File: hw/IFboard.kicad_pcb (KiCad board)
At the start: 2 copper layers, 110 x 65.1 mm, 99 parts, among them J1 USB_C_Receptacle_USB2.0_16P, J10 IcoTec_36650.2, J2 Phoenix_1881561, J3 Conn_ARM_SWD_TagConnect_TC203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, J4 Phoenix_1881561, J5 Phoenix_1881561, J6 Phoenix_1881561, J7 IcoTec_36650.2, J8 IcoTec_36650.2, J9 IcoTec_36650.2, SW3 SW_Push, SW4 SW_Push, SW5 SW_Push, SW6 SW_Push, U2 XC6206P332MR-G, U3 TCAN3413DR, U4 ST4E1240DT, U5 MAX232ESE+T, U6 STM32G0B1CBTx, U7 ER_OLEDM0.91_1x-I2C

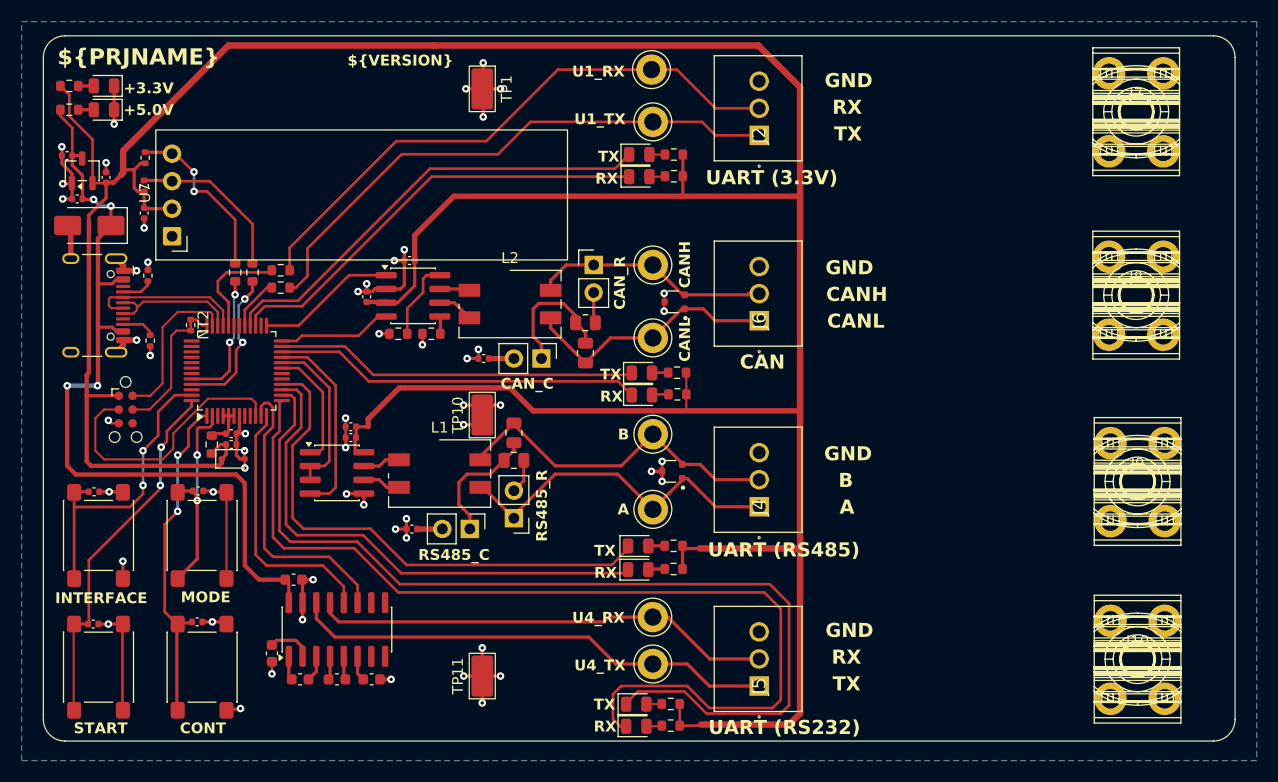
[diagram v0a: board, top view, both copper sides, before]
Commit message: added jumpers to be able to short CMCs
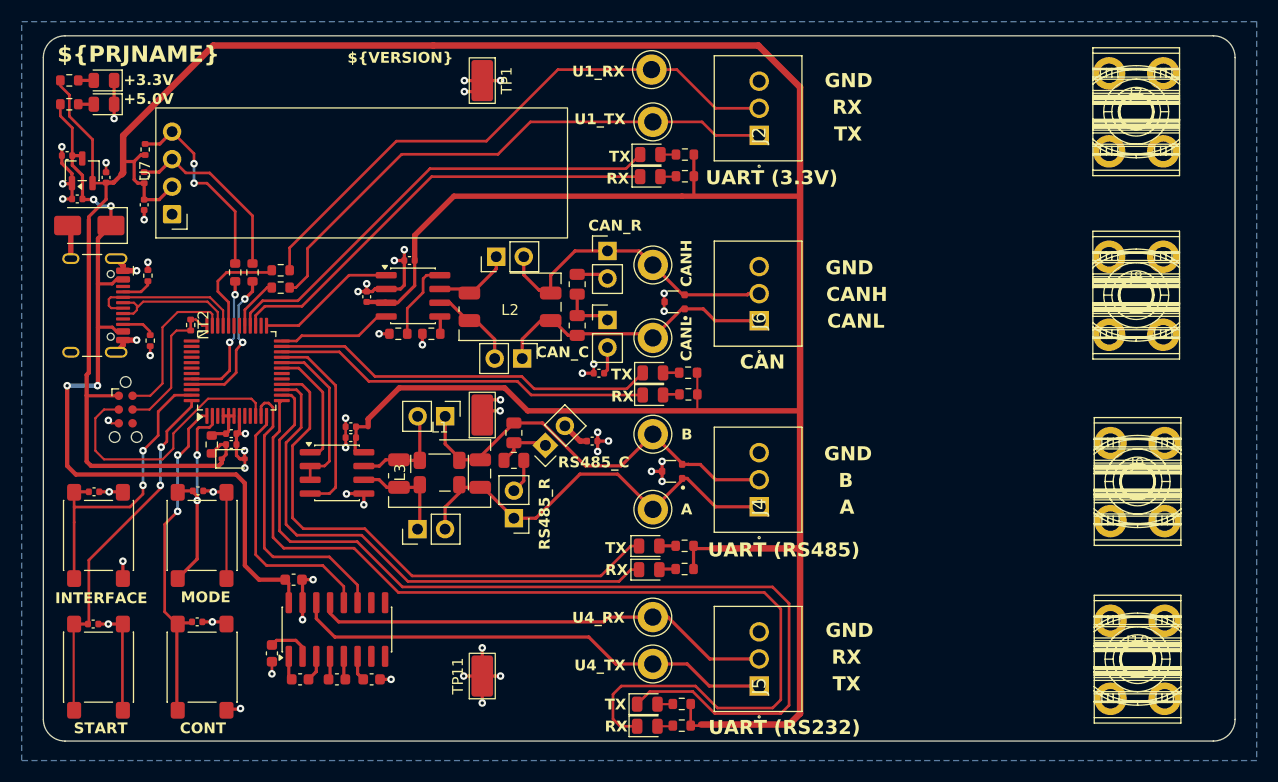
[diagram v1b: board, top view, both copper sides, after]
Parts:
- added JP5: Jumper_2_Open, Connector_PinHeader_2.54mm:PinHeader_1x02_P2.54mm_Vertical, F.Cu at (85.5, 95.9)
- added JP6: Jumper_2_Open, Connector_PinHeader_2.54mm:PinHeader_1x02_P2.54mm_Vertical, F.Cu at (88.0, 85.5)
- added JP7: Jumper_2_Open, Connector_PinHeader_2.54mm:PinHeader_1x02_P2.54mm_Vertical, F.Cu at (92.7, 70.7)
- added JP8: Jumper_2_Open, Connector_PinHeader_2.54mm:PinHeader_1x02_P2.54mm_Vertical, F.Cu at (95.1, 80.1)
- added L3: 100 uH, PZ:L_Wurth_WE-CNSW-1812, F.Cu at (87.5, 90.6)
- moved C24 18.5 mm to (101.6, 87.7), turned to 180 degrees
- moved C20 10.7 mm to (102.2, 81.5)
- moved JP3 10.4 mm to (97.3, 88.1), turned to 135 degrees
- moved JP4 7.06 mm to (103.0, 76.6), turned to 0 degrees
- moved R14 3.64 mm to (100.2, 73.3), turned to -90 degrees
- moved R15 2.65 mm to (100.2, 77.1)
- moved U7 2.03 mm to (62.8, 66.8)
- moved JP2 1.82 mm to (103.0, 70.2)
- moved D10 1.02 mm to (106.8, 99.6)
- moved D6 1.02 mm to (107.2, 81.4)
- moved D8 1.02 mm to (107.2, 83.5)
- moved D9 1.02 mm to (106.8, 97.4)
- moved R10 1.02 mm to (110.1, 61.3)
- moved R11 1.02 mm to (110.1, 63.3)
- moved R13 1.02 mm to (110.5, 83.4)
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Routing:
- net Net-(JP4-A): track 12.4 -> 4.69 mm
- net GND: track 115.2 -> 107.8 mm, vias 55 -> 53
- net Net-(JP3-A): track 11.7 -> 5.01 mm
- net Net-(J4-Pin_2): track 32.1 -> 38.7 mm
- net Net-(J4-Pin_1): track 32.7 -> 39.2 mm
- net Net-(JP5-A): track 3.54 -> 9.75 mm
- net Net-(J6-Pin_2): track 21.9 -> 28.0 mm
- net Net-(JP6-B): track 3.48 -> 9.57 mm
- net Net-(JP8-B): track 3.31 -> 8.24 mm
- net Net-(JP7-A): track 2.78 -> 7.56 mm
- net Net-(J6-Pin_1): track 24.0 -> 26.9 mm
- net /SDA: track 16.0 -> 18.3 mm
- net /CAN_TX_LED: track 33.5 -> 35.5 mm
- net /USART3_TX_LED: track 48.5 -> 50.5 mm
- net /SCL: track 15.2 -> 17.1 mm
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
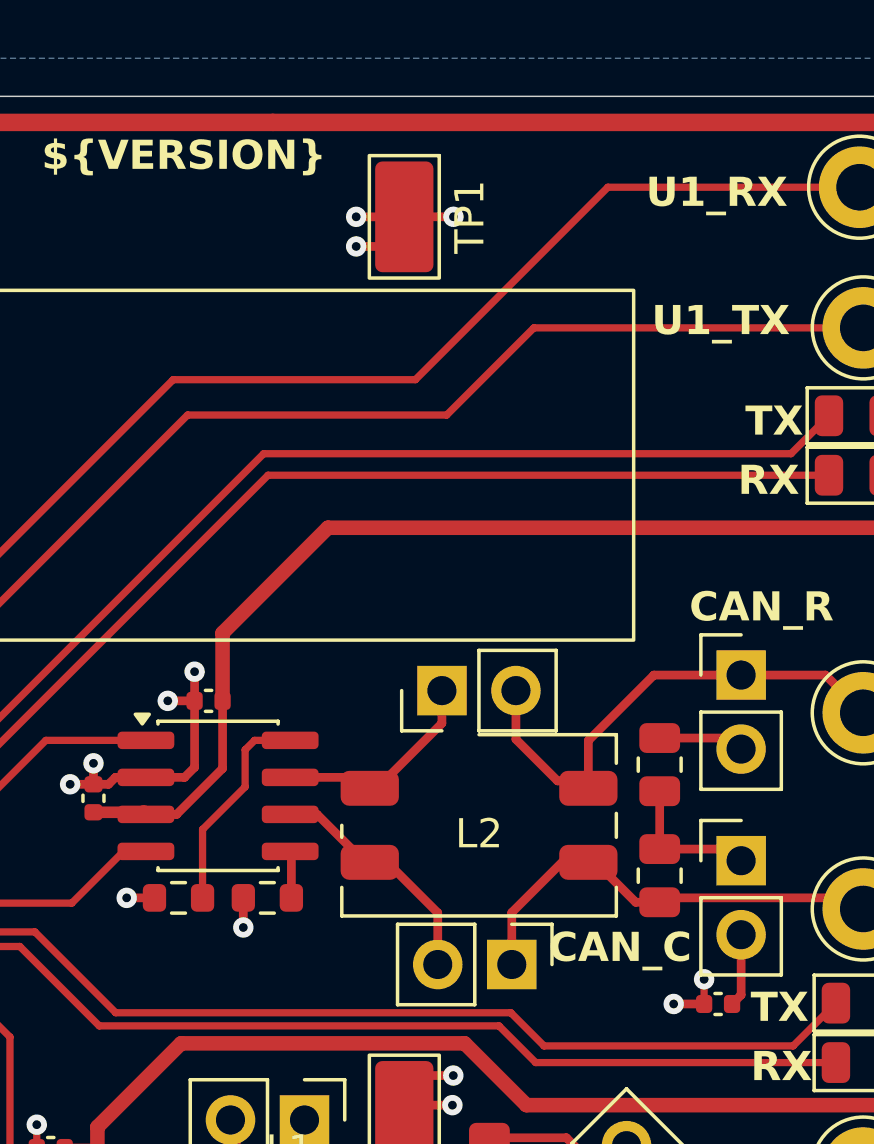
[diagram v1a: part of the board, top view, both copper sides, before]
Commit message: corrected rotation offsets for JLC
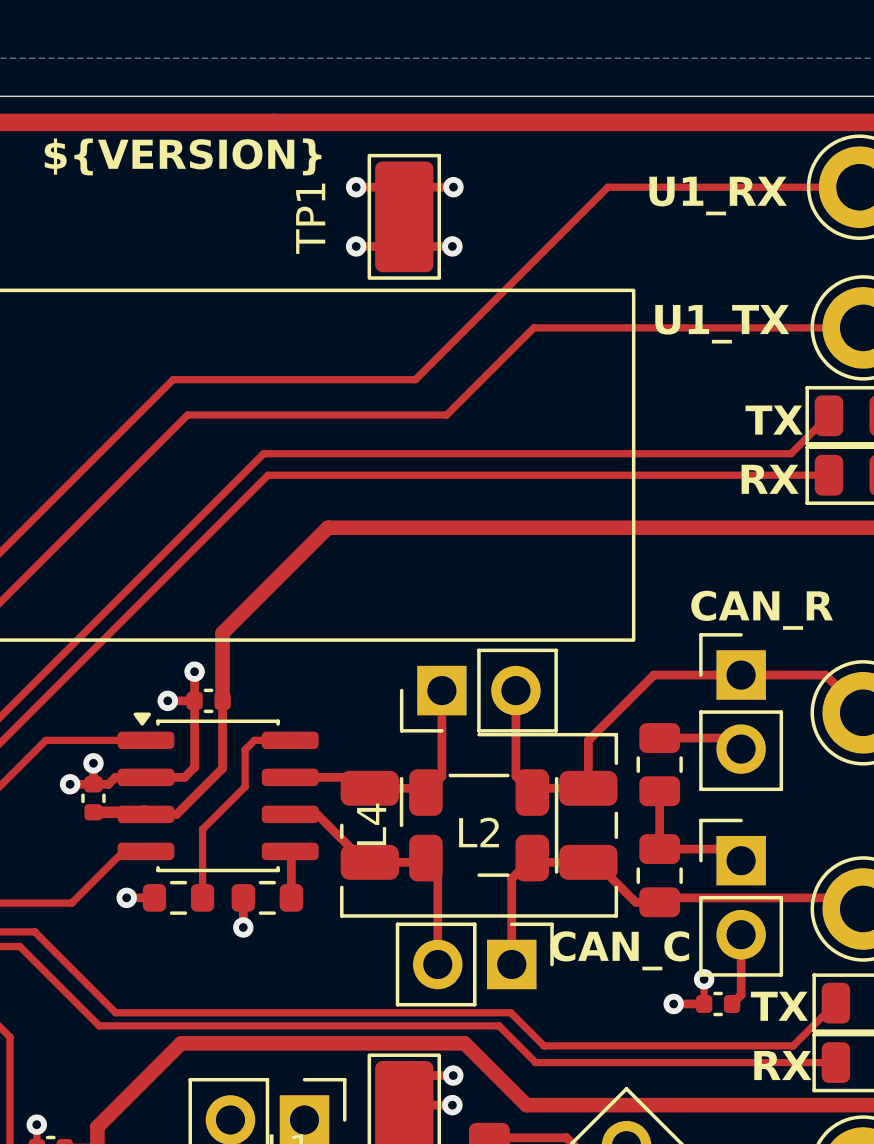
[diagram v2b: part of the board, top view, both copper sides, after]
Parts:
- added L4: 100 uH, PZ:L_Wurth_WE-CNSW-1812, F.Cu at (94.0, 75.3)
- turned TP3 to 0 degrees
- turned TP5 to 0 degrees
- turned TP6 to 0 degrees
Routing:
- net GND: track 107.8 -> 109.5 mm, vias 53 -> 54
- net Net-(JP8-B): track 8.24 -> 9.46 mm
- net Net-(JP7-A): track 7.56 -> 8.75 mm
- net Net-(J6-Pin_2): track 28.0 -> 29.0 mm
- net Net-(J6-Pin_1): track 26.9 -> 27.6 mm

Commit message: first version sent to JLC
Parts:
- added BZ1: CPT-9019S-SMT-TR, PZ:Buzzer_CUI_CPT-9019S-SMT, F.Cu at (75.8, 110.3)
- added C26: 1u, Capacitor_SMD:C_0402_1005Metric, F.Cu at (79.9, 105.0)
- added D15: PESD2CANFD24V-UX, PZ:TVS_PESD2CANFD24V-UX, F.Cu at (110.6, 106.3)
- added D16: PESD3V3U1UA, Diode_SMD:D_SOD-323, F.Cu at (110.4, 54.5)
- added D17: PESD3V3U1UA, Diode_SMD:D_SOD-323, F.Cu at (110.4, 57.8)
- added Q1: MMBT3904, Package_TO_SOT_SMD:SOT-23, F.Cu at (74.8, 103.5)
- added R29: 1k, Resistor_SMD:R_0603_1608Metric, F.Cu at (72.0, 103.5)
- added TP12: TestPoint_Keystone_5019, PZ:TestPoint_Keystone_5019_Miniature, F.Cu at (87.5, 54.2)
- added TP13: TestPoint_Keystone_5019, PZ:TestPoint_Keystone_5019_Miniature, F.Cu at (137.5, 82.7)
- added TP14: TestPoint_Keystone_5019, PZ:TestPoint_Keystone_5019_Miniature, F.Cu at (137.5, 112.5)
- added TP15: TestPoint_Keystone_5019, PZ:TestPoint_Keystone_5019_Miniature, F.Cu at (137.5, 53.6)
- C20, C24: footprint Capacitor_SMD:C_0402_1005Metric -> Capacitor_SMD:C_0603_1608Metric
- moved TP10 19.5 mm to (96.6, 104.1)
- moved C13 10.9 mm to (82.6, 110.1)
- moved C10 10.9 mm to (85.2, 112.5)
- moved C11 10.9 mm to (88.6, 112.5)
- moved C12 10.9 mm to (84.6, 103.3)
- moved C14 10.9 mm to (91.8, 112.5)
- moved U5 10.9 mm to (88.6, 107.9)
- moved TP11 5.67 mm to (96.6, 111.7)
- moved TP1 4.20 mm to (95.6, 54.2)
- moved C20 0.80 mm to (101.4, 81.7)
- moved J3 0.76 mm to (57.8, 84.8)
- moved C24 0.57 mm to (102.1, 88.0)
- moved JP3 0.57 mm to (97.8, 88.4)
- turned TP2 to 90 degrees
- turned TP3 to 90 degrees
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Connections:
- U6 pad 42: unconnected-(U6-PB3-Pad42) -> /BUZZER
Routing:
- net GND: track 109.5 -> 146.1 mm, vias 54 -> 81
- net /BUZZER: track 0.00 -> 35.4 mm, vias 0 -> 4
- net VBUS: track 77.3 -> 95.9 mm
- net /USART4_TX: track 27.3 -> 39.6 mm
- net /USART4_RX: track 24.1 -> 35.9 mm
- net /USART4_TX_MAX: track 44.9 -> 35.0 mm
- net /USART4_RX_MAX: track 42.7 -> 33.9 mm
- net Net-(BZ1--): track 0.00 -> 8.48 mm
- net Net-(Q1-B): track 0.00 -> 2.59 mm
- net /USART3_TX_LED: track 50.5 -> 49.0 mm
- net /NRST: track 25.1 -> 26.3 mm
- net +3.3V: track 323.9 -> 324.9 mm
- net /USART3_RX_LED: track 49.8 -> 48.9 mm
- net Net-(JP3-B): track 2.62 -> 1.98 mm
- net Net-(J4-Pin_2): track 38.7 -> 38.1 mm
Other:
- board text added: "${PRJNAME} ${VERSION}"
- board text removed: "${PRJNAME}"
- board text removed: "${VERSION}"
